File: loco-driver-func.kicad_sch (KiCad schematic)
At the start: 5 parts, among them Q201 BSS138, Q202 BSS138

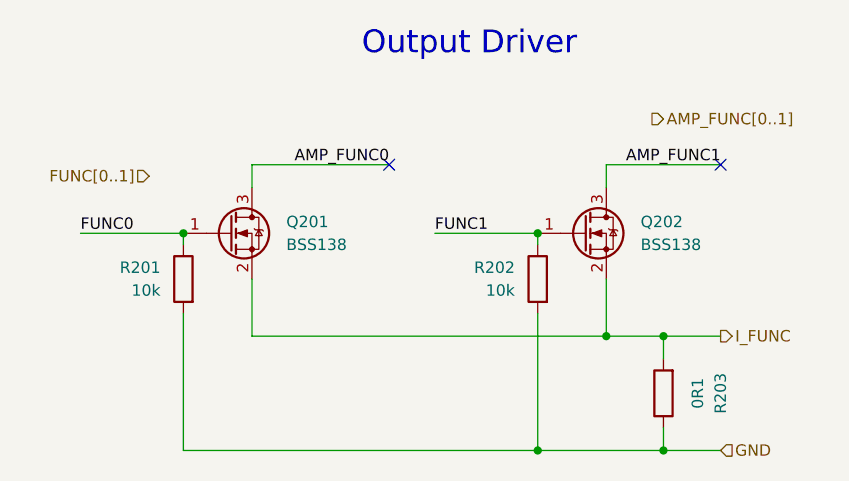
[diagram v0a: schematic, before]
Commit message: Fix - Ignore double power flags
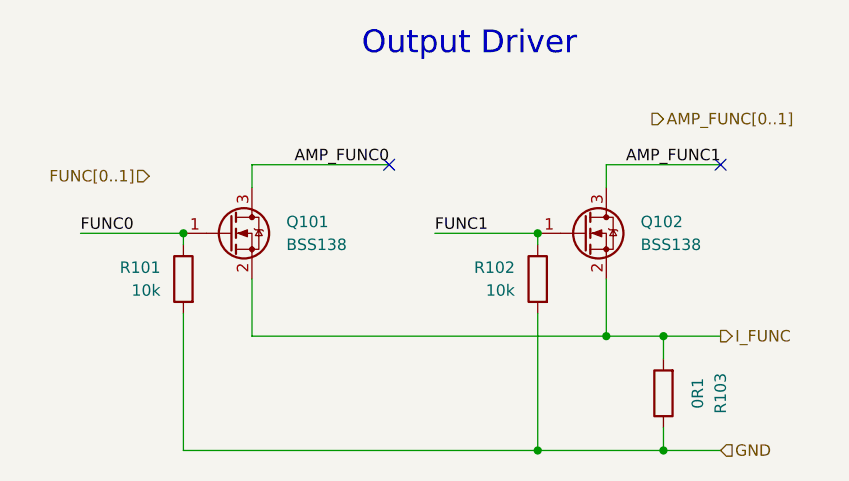
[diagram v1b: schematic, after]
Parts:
- renumbered Q201 to Q101, Q202 to Q102, R201 to R101, R202 to R102, R203 to R103
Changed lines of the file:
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@@
+		)
+	)
+	(hierarchical_label "I_FUNC"
+		(shape output)
+		(at 99.06 67.31 0)
+		(effects
+			(font
+				(size 1.27 1.27)
+			)
+			(justify left)
 		)
 	)
@@
 		(shape input)
 		(at 99.06 80.01 0)
-		(effects
-			(font
-				(size 1.27 1.27)
-			)
-			(justify left)
-		)
-	)
-	(hierarchical_label "I_FUNC"
-		(shape output)
-		(at 99.06 67.31 0)
 		(effects
 			(font
@@
 		(on_board yes)
 		(dnp no)
-		(property "Reference" "R202"
+		(property "Reference" "R102"
 			(at 76.2 59.6899 0)
 			(effects
@@
 			(project "xDuinoRails-Thor-M"
 				(path "/fb33ec4e-6596-45d2-a121-8d3475acd69a/e1a52612-70a7-429e-ada6-6f2a698a279c"
-					(reference "R902")
+					(reference "R1002")
 					(unit 1)
 				)
@@
 		(on_board yes)
 		(dnp no)
-		(property "Reference" "R203"
+		(property "Reference" "R103"
 			(at 99.06 73.66 90)
 			(effects
@@
 			(project "xDuinoRails-Thor-M"
 				(path "/fb33ec4e-6596-45d2-a121-8d3475acd69a/e1a52612-70a7-429e-ada6-6f2a698a279c"
-					(reference "R903")
+					(reference "R1003")
 					(unit 1)
 				)
@@
 		(on_board yes)
 		(dnp no)
-		(property "Reference" "R201"
+		(property "Reference" "R101"
 			(at 36.83 59.6899 0)
 			(effects
@@
 			(project "xDuinoRails-Thor-M"
 				(path "/fb33ec4e-6596-45d2-a121-8d3475acd69a/e1a52612-70a7-429e-ada6-6f2a698a279c"
-					(reference "R901")
+					(reference "R1001")
 					(unit 1)
 				)
@@
 		(dnp no)
 		(fields_autoplaced yes)
-		(property "Reference" "Q201"
+		(property "Reference" "Q101"
 			(at 50.8 54.6099 0)
 			(effects
@@
 			(project "xDuinoRails-Thor-M"
 				(path "/fb33ec4e-6596-45d2-a121-8d3475acd69a/e1a52612-70a7-429e-ada6-6f2a698a279c"
-					(reference "Q901")
+					(reference "Q1001")
 					(unit 1)
 				)
@@
 		(dnp no)
 		(fields_autoplaced yes)
-		(property "Reference" "Q202"
+		(property "Reference" "Q102"
 			(at 90.17 54.6099 0)
 			(effects
@@
 			(project "xDuinoRails-Thor-M"
 				(path "/fb33ec4e-6596-45d2-a121-8d3475acd69a/e1a52612-70a7-429e-ada6-6f2a698a279c"
-					(reference "Q902")
-					(unit 1)
-				)
+					(reference "Q1002")
+					(unit 1)
+				)
